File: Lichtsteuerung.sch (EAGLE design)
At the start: 188 parts, among them IC1 74HC595D, IC10 TSR_1-2450, IC11 MEGA64-A, IC12 75176AD, IC13 DS1307SO8, IC2 74HC595D, IC3 74HC595D, IC4 74HC595D, IC5 75176AD, IC6 MEGA168-AI, IC9 24FC128-I/SN, Q1 32.768, Q2 16MHz, Q3 16MHz, U1 MAX232SOIC16, X1 713-1410, X2 713-1410, X3 733-333, X4 733-332, X5 713-1410, X6 733-334, X7 733-333, X8 733-333

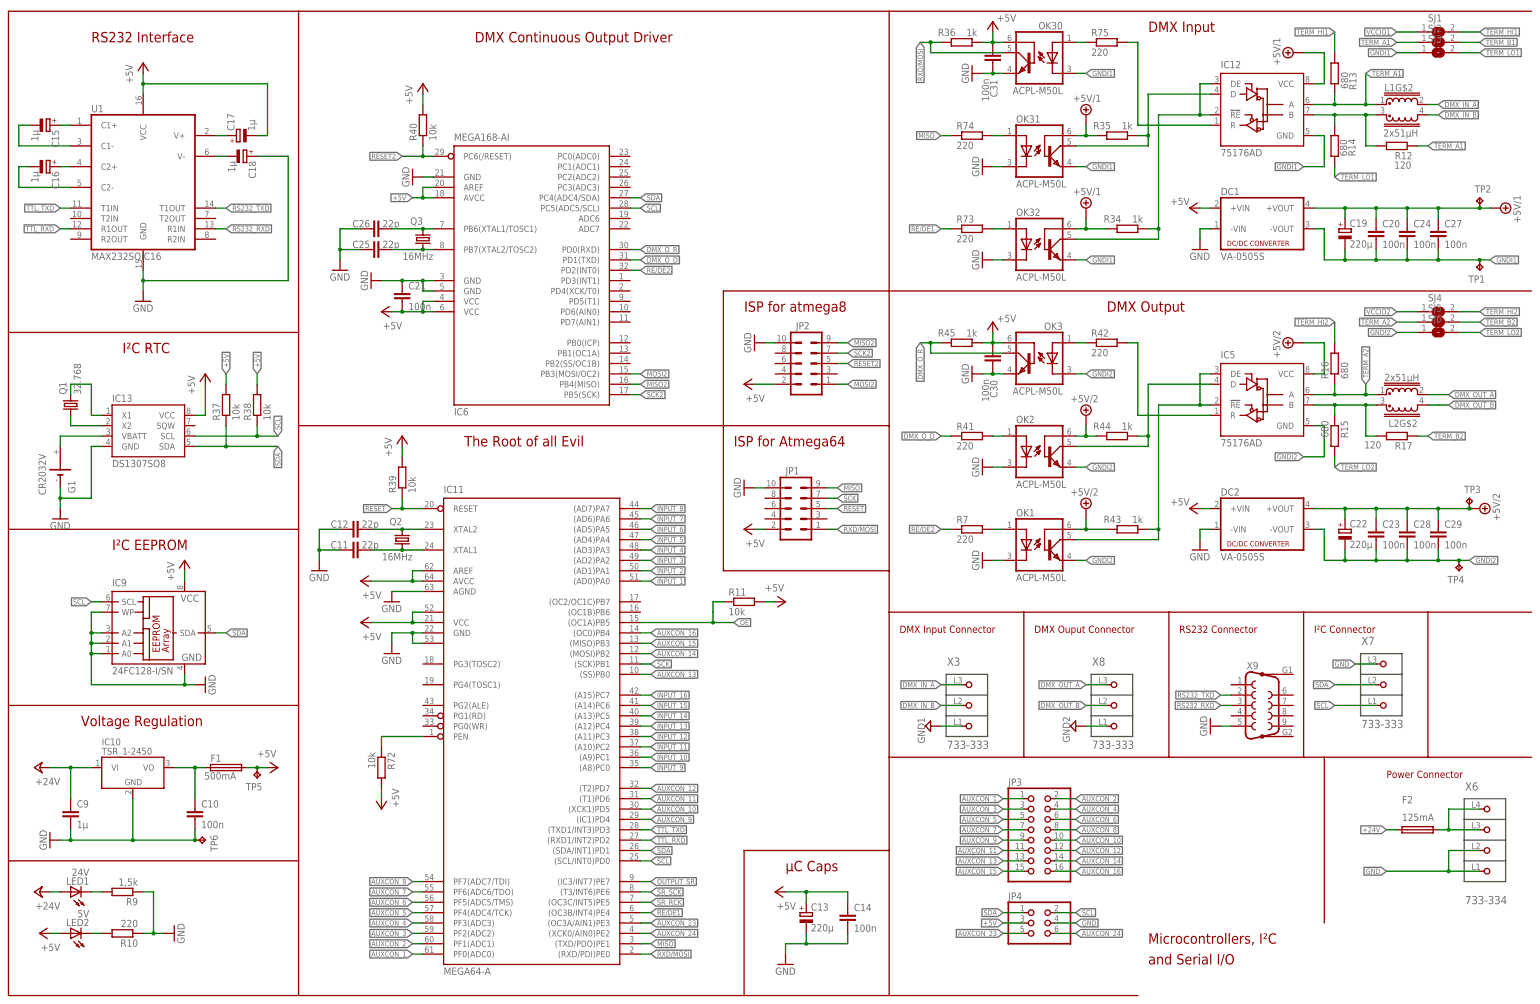
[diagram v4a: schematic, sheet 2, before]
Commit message: Initial revision F
Changes:
* Removed Atmega8 + second RS485 interface, because we're using an RS485 hub and RDM instead
* Added more (software controlled) status LEDs
* Added optional external VCC for the relais drivers
* Replaced SMD solder jumpers with real jumpers for DMX Term / Pull Up / Pull Down
* All components placed now on the first layer, in order to allow reflowing of the components
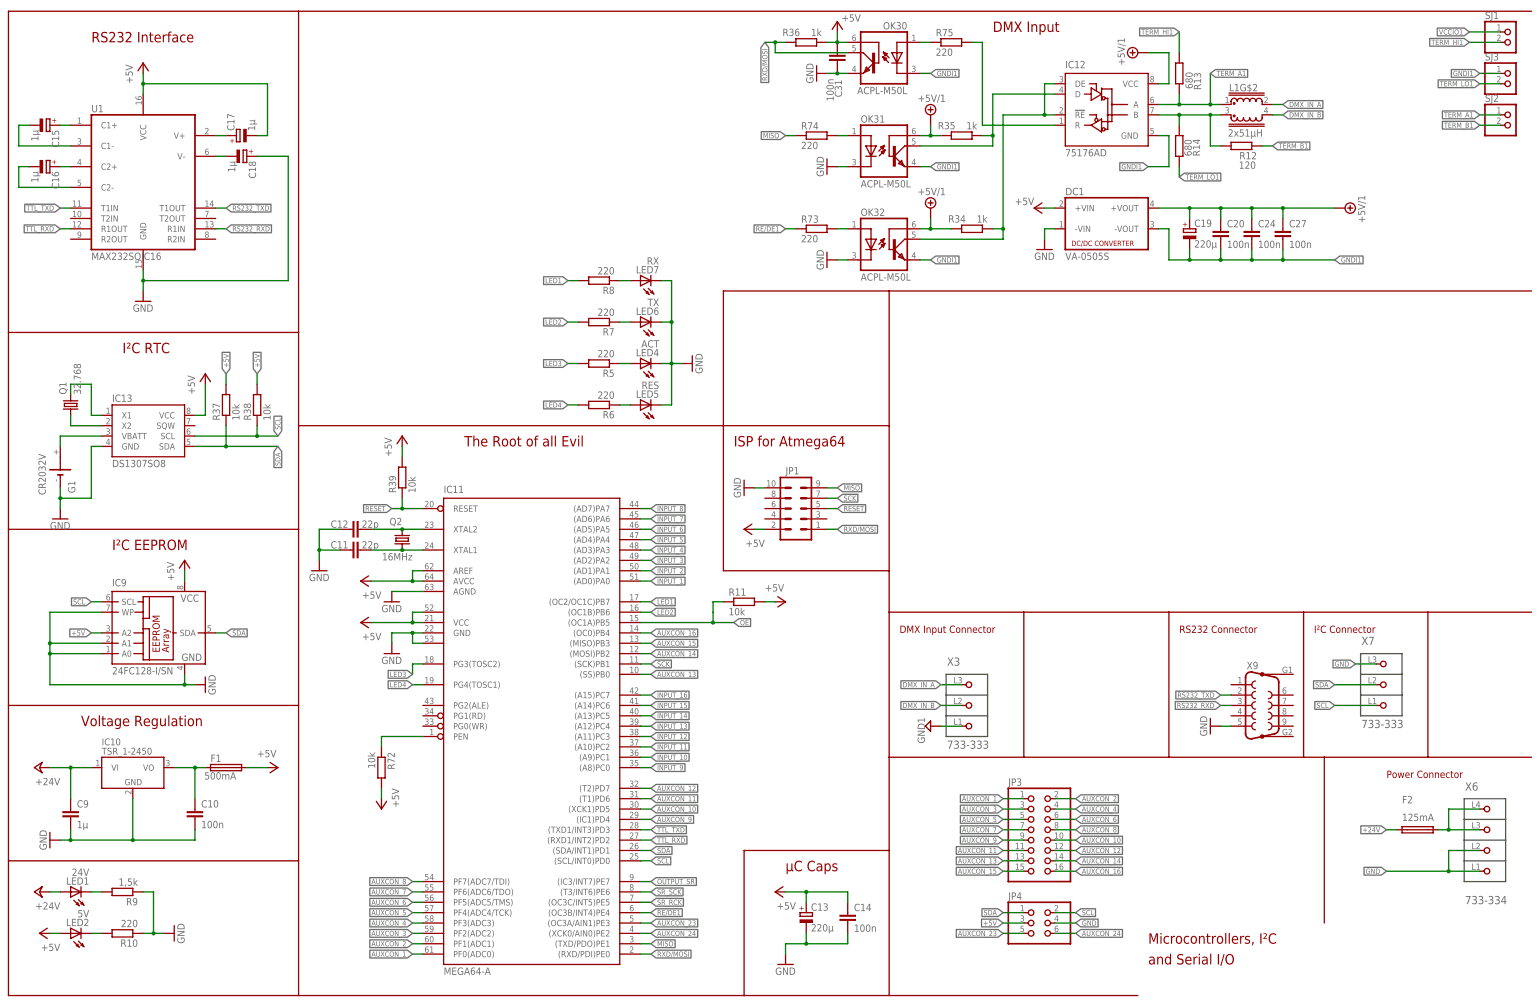
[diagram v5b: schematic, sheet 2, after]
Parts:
- removed C21: 100n, resistor:C-EUC0805
- removed C22: 220µ, rcl:CPOL-EUD
- removed C23, C28, C29, C30: 100n, rcl:C-EUC0805
- removed C25, C26: 22p, rcl:C-EUC0805
- removed DC2: VA-0505S, dc-dc-converter:VA-0505S
- removed IC5: 75176AD, 751xx:75176AD
- removed IC6: MEGA168-AI, atmel:MEGA8-AI
- removed L2: 2x51µH, epcos-b82790c0:EPCOS_B82790C0
- removed OK1, OK2, OK3: ACPL-M50L, ACPL-M50L:ACPL-M50L
- removed Q3: 16MHz, Crystals-new:CRYSTALMJ
- removed R15, R16: 680, rcl:R-EU_R0805
- removed R17: 120, rcl:R-EU_R0805
- removed R40: 10k, resistor:R-EU_R0805
- removed R41, R42: 220, resistor:R-EU_R0805
- removed R43, R44, R45: 1k, resistor:R-EU_R0805
- removed SJ4, SJ5, SJ6: (no value), jumper:SJ
- removed TP1, TP2, TP3, TP4, TP5, TP6: TPPAD1-13, testpad:TPPAD1-13
- removed X8: 733-333, con-wago_2.5mm:733-333
- added JP6: (no value), pinhead:PINHD-1X2
- added LED4: ACT, led:LEDCHIP-LED0805
- added LED5: RES, led:LEDCHIP-LED0805
- added LED6: TX, led:LEDCHIP-LED0805
- added LED7: RX, led:LEDCHIP-LED0805
- added R5, R6, R8: 220, rcl:R-EU_R0805
- C13, C19: device rcl:CPOL-EUD -> rcl:CPOL-EUC/6032-28R
- C15, C16, C17, C18: device rcl:CPOL-EU153CLV-0405 -> resistor:CPOL-EUA/3216-18R
- JP2: device con-ml:ML10 -> pinhead:PINHD-1X2; OC_REICHELT WSL 10G -> (none)
- R7: device resistor:R-EU_R0805 -> rcl:R-EU_R0805
- SJ1, SJ2, SJ3: device jumper:SJ -> pinhead:PINHD-1X2
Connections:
- removed net DMX_OUT_A: L2G$1.4, X8.P3
- removed net DMX_OUT_B: L2G$2.4, X8.P2
- removed net DMX_O_D: IC6.PD1(TXD), R41.1
- removed net DMX_O_R: IC6.PD0(RXD), OK3.COL, R45.2
- removed net GNDI2: C22.-, C23.2, C28.2, C29.2, DC2.-VOUT, IC5.GND, OK1.EMI, OK2.EMI, OK3.C, SJ6.1, TP4.TP, X8.P1
- removed net MISO2: IC6.PB4(MISO), JP2.9
- removed net MOSI2: IC6.PB3(MOSI/OC2), JP2.1
- removed net N$79: OK1.A, R7.2
- removed net N$88: IC5.B, L2G$2.1, R15.1, R17.2
- removed net RE/DE2: IC6.PD2(INT0), R7.1
- removed net REC$3: IC5.R, R42.2
- removed net RESET2: IC6.PC6(/RESET), JP2.5, R40.1
- removed net RE_OUT2: IC5.!RE, IC5.DE, OK1.COL, R43.1
- removed net SCK2: IC6.PB5(SCK), JP2.7
- removed net TERM_A2: IC5.A, L2G$1.1, R16.1, SJ5.1
- removed net TERM_B2: R17.1, SJ5.2
- removed net TERM_HI2: R16.2, SJ4.2
- removed net TERM_LO2: R15.2, SJ6.2
- removed net TXD_OUT2: IC5.D, OK2.COL, R44.1
- removed net VCCIO2: C22.+, C23.1, C28.1, C29.1, DC2.+VOUT, IC5.VCC, OK1.BAS, OK2.BAS, R43.2, R44.2, SJ4.1, TP3.TP
- new net LED1: IC11.(OC2/OC1C)PB7, R8.2
- new net LED2: IC11.(OC1B)PB6, R7.2
- new net LED3: IC11.PG3(TOSC2), R5.2
- new net LED4: IC11.PG4(TOSC1), R6.2
- new net N$48: LED6.A, R7.1
- new net N$53: LED4.A, R5.1
- net +24V: now also JP2.2, JP6.2; no longer C1.1, C2.1, C3.1, C4.1, F3.2, F4.1, ULN1.10, ULN2.10, ULN3.10, ULN4.10
- net +24V_01: now also C1.1, C2.1, ULN1.10, ULN2.10
- net +24V_02: now also C3.1, C4.1, ULN3.10, ULN4.10
- net +5V: now also IC9.A2; no longer C21.2, C30.1, DC2.+VIN, IC6.AREF, IC6.AVCC, IC6.VCC@1, IC6.VCC@2, JP2.2, OK3.BAS, R40.2, R45.1, TP5.TP
- net GND: now also LED4.C, LED5.C, LED6.C, LED7.C; no longer C21.1, C25.2, C26.2, C30.2, DC2.-VIN, IC6.GND, IC6.GND@1, IC6.GND@2, IC9.A2, JP2.10, OK1.C, OK2.C, OK3.EMI, TP6.TP
- net GNDI1: no longer TP1.TP
- net N$45: now also LED7.A, R8.1; no longer OK3.A, R42.1
- net N$73: now also LED5.A, R6.1; no longer OK2.A, R41.2
- net N$74: now also F4.1, JP6.1; no longer C25.1, IC6.PB7(XTAL2/TOSC2), Q3G$1.2
- net N$76: now also F3.2, JP2.1; no longer C26.1, IC6.PB6(XTAL1/TOSC1), Q3G$1.1
- net SCL: no longer IC6.PC5(ADC5/SCL)
- net SDA: no longer IC6.PC4(ADC4/SDA)
- net TERM_A1: no longer R12.1
- net TERM_B1: now also R12.1
- net VCCIO1: no longer TP2.TP
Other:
- note removed: "DMX Continuous Output Driver"
- note removed: "DMX Ouput Connector"
- note removed: "DMX Output"
- note removed: "ISP for atmega8"
- moved on the sheet: C19, C20, C24, C27, C31, DC1, F3, F4, IC12, L1G$2, OK30, OK31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

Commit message: Finalized Revision F
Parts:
- removed LED7: RX, led:LEDCHIP-LED0805
- removed SJ1, SJ2, SJ3: (no value), pinhead:PINHD-1X2
- added J1, J2, J3: (no value), pinhead:PINHD-1X2
- added LED3: ACT, led:LEDCHIP-LED0805
- LED1: value 24V -> 5V; OC_REICHELT SMD-LED 0805 RT -> SMD-LED 0805 GE
- LED2: value 5V -> 24V; OC_REICHELT SMD-LED 0805 GE -> SMD-LED 0805 RT
- LED4: value ACT -> RES
- LED5: value RES -> TX
- LED6: value TX -> RX
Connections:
- removed net N$80: LED1.C, R9.2
- removed net N$82: LED2.C, R10.2
- new net N$77: LED1.A, R10.1
- new net N$79: LED2.A, R9.1
- net +24V: now also R9.2; no longer LED1.A
- net +5V: now also R10.2; no longer LED2.A
- net GND: now also LED1.C, LED2.C, LED3.C; no longer LED7.C, R10.1, R9.1
- net GNDI1: now also J1.1; no longer SJ3.1
- net N$45: now also LED6.A; no longer LED7.A
- net N$48: now also LED5.A; no longer LED6.A
- net N$53: now also LED3.A; no longer LED4.A
- net N$73: now also LED4.A; no longer LED5.A
- net TERM_A1: now also J3.1; no longer SJ2.1
- net TERM_B1: now also J3.2; no longer SJ2.2
- net TERM_HI1: now also J2.2; no longer SJ1.2
- net TERM_LO1: now also J1.2; no longer SJ3.2
- net VCCIO1: now also J2.1; no longer SJ1.1
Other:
- moved on the sheet: LED1, LED2, LED4, LED5, LED6, R10, R9

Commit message: Additions: - Added POWER OK LEDs for the inputs/outputs with constant current source (in case we need to connect other voltages and a fixed resistors won't help) - Added test points for all major signals and voltages - Added Logo
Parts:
- added IC5, IC6, IC7: LM317LD, linear:LM317LD
- added JP10: PINHD-1X10, adafruit:PINHD-1X10
- added JP7: (no value), pinhead:PINHD-1X2
- added LED7, LED8, LED9: PWROK, led:LEDCHIP-LED0805
- added R15, R16, R17: 125, resistor:R-EU_R0805
- F1: value 500mA -> 5V Rail 500mA
- F2: value 125mA -> 24V Rail 250mA
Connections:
- new net N$80: IC5.ADJ, R16.1
- new net N$82: IC5.VO, IC5.VO@1, IC5.VO@2, IC5.VO@3, LED8.A, R16.2
- new net N$83: IC7.ADJ, R17.1
- new net N$85: IC6.ADJ, R15.1
- new net N$86: IC6.VO, IC6.VO@1, IC6.VO@2, IC6.VO@3, LED7.A, R15.2
- new net N$88: IC7.VO, IC7.VO@1, IC7.VO@2, IC7.VO@3, LED9.A, R17.2
- net +24V: now also JP10.2
- net +24V_01: now also IC6.VI
- net +24V_02: now also IC5.VI
- net +24V_03: now also IC7.VI
- net +5V: now also JP10.1
- net DMX_IN_A: now also JP10.8
- net DMX_IN_B: now also JP10.9
- net GND: now also JP10.3, JP7.1, LED7.C, LED8.C
- net GNDI1: now also JP10.10
- net GNDINT: now also JP10.4, JP7.2, LED9.C
- net SCL: now also JP10.7
- net SDA: now also JP10.6
- net VCCIO1: now also JP10.5
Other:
- moved on the sheet: C5, C6, C7, C8, F3, F4, IC1P, IC2P, IC3P, IC4P, JP2, JP5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

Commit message: Updated part ordering numbers, added connector plugs and case to the BOM
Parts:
- C11, C12: OC_REICHELT X7R-G0805 22P -> NPO-G0805 22P
- C13, C19: value 220µ -> 10µ; OC_REICHELT VF 220/6,3 K-D -> (none); PARTKEEPR_SKU (none) -> 2607
- C15, C16, C17, C18: OC_REICHELT VF 1,0/50 C-B -> (none); PARTKEEPR_SKU (none) -> 2609
- IC11: OC_REICHELT ATMEGA 64-16 TQ -> ATMEGA 2561-16AU
- IC5, IC6, IC7: OC_REICHELT (none) -> LM 317 LD
- IC9: OC_REICHELT 24FC128-I/SN -> 24FC1025-I/SM
- OK116: OC_REICHELT (none) -> LTV 356T-SMD
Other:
- note added: "Connectors and other auxiliary parts"
- note added: "Constant Current Source with LM317, based on App Note AND8109/D by ON Semiconductor. The reason we do this is because we don't know the voltage applied to the +24V rails fed in externally, which may be anything from 4 to 30V."
